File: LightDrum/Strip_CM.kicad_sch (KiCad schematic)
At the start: 10 parts, among them U42 INA4181 A2, U43 INA4181 A2

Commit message: Add docs and gerbers for REV7
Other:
- title: RGB CURRENT MONITORS -> LightDrum
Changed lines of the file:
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@@
   (paper "A4")
   (title_block
-    (title "RGB CURRENT MONITORS")
-    (rev "REV6")
+    (title "LightDrum")
+    (rev "REV7")
     (company "Daxxn Industries")
   )

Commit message: First pass over schematic (WIP)
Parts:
- R108, R109, R110, R111, R112, R113, R114, R115: value 60m${RES} -> 60m
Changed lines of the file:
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@@
   (title_block
     (title "LightDrum")
-    (rev "REV7")
+    (rev "REV8")
     (company "Daxxn Industries")
   )
@@
       (effects (font (size 1.27 1.27)) hide)
     )
-    (property "Datasheet" "C:\\Users\\Daxxn\\Documents\\Electrical\\Datasheets\\INA181.pdf" (id 3) (at 90.17 53.34 0)
+    (property "Datasheet" "%LOCAL_DATASHEETS%\\INA181.pdf" (id 3) (at 90.17 53.34 0)
       (effects (font (size 1.27 1.27)) hide)
     )
@@
     (in_bom yes) (on_board yes)
     (property "Reference" "R115" (id 0) (at 77.47 102.87 90))
-    (property "Value" "60m${RES}" (id 1) (at 77.47 104.648 90))
+    (property "Value" "60m" (id 1) (at 77.47 104.648 90))
     (property "Footprint" "Resistor_SMD:R_2010_5025Metric" (id 2) (at 77.724 105.664 90)
       (effects (font (size 1.27 1.27)) hide)
@@
     (in_bom yes) (on_board yes)
     (property "Reference" "R114" (id 0) (at 77.47 77.47 90))
-    (property "Value" "60m${RES}" (id 1) (at 77.47 79.248 90))
+    (property "Value" "60m" (id 1) (at 77.47 79.248 90))
     (property "Footprint" "Resistor_SMD:R_2010_5025Metric" (id 2) (at 77.724 80.264 90)
       (effects (font (size 1.27 1.27)) hide)
@@
       (effects (font (size 1.27 1.27)) hide)
     )
-    (property "Datasheet" "C:\\Users\\Daxxn\\Documents\\Electrical\\Datasheets\\INA181.pdf" (id 3) (at 90.17 27.94 0)
+    (property "Datasheet" "%LOCAL_DATASHEETS%\\INA181.pdf" (id 3) (at 90.17 27.94 0)
       (effects (font (size 1.27 1.27)) hide)
     )
@@
       (effects (font (size 1.27 1.27)) hide)
     )
-    (property "Datasheet" "C:\\Users\\Daxxn\\Documents\\Electrical\\Datasheets\\INA181.pdf" (id 3) (at 39.37 27.94 0)
+    (property "Datasheet" "%LOCAL_DATASHEETS%\\INA181.pdf" (id 3) (at 39.37 27.94 0)
       (effects (font (size 1.27 1.27)) hide)
     )
@@
     (in_bom yes) (on_board yes)
     (property "Reference" "R110" (id 0) (at 26.67 77.47 90))
-    (property "Value" "60m${RES}" (id 1) (at 26.67 79.248 90))
+    (property "Value" "60m" (id 1) (at 26.67 79.248 90))
     (property "Footprint" "Resistor_SMD:R_2010_5025Metric" (id 2) (at 26.924 80.264 90)
       (effects (font (size 1.27 1.27)) hide)
@@
       (effects (font (size 1.27 1.27)) hide)
     )
-    (property "Datasheet" "C:\\Users\\Daxxn\\Documents\\Electrical\\Datasheets\\INA181.pdf" (id 3) (at 39.37 104.14 0)
+    (property "Datasheet" "%LOCAL_DATASHEETS%\\INA181.pdf" (id 3) (at 39.37 104.14 0)
       (effects (font (size 1.27 1.27)) hide)
     )
@@
       (effects (font (size 1.27 1.27)) hide)
     )
-    (property "Datasheet" "C:\\Users\\Daxxn\\Documents\\Electrical\\Datasheets\\INA181.pdf" (id 3) (at 90.17 78.74 0)
+    (property "Datasheet" "%LOCAL_DATASHEETS%\\INA181.pdf" (id 3) (at 90.17 78.74 0)
       (effects (font (size 1.27 1.27)) hide)
     )
@@
     (in_bom yes) (on_board yes)
     (property "Reference" "R113" (id 0) (at 77.47 52.07 90))
-    (property "Value" "60m${RES}" (id 1) (at 77.47 53.848 90))
+    (property "Value" "60m" (id 1) (at 77.47 53.848 90))
     (property "Footprint" "Resistor_SMD:R_2010_5025Metric" (id 2) (at 77.724 54.864 90)
       (effects (font (size 1.27 1.27)) hide)
@@
       (effects (font (size 1.27 1.27)) hide)
     )
-    (property "Datasheet" "C:\\Users\\Daxxn\\Documents\\Electrical\\Datasheets\\INA181.pdf" (id 3) (at 90.17 104.14 0)
+    (property "Datasheet" "%LOCAL_DATASHEETS%\\INA181.pdf" (id 3) (at 90.17 104.14 0)
       (effects (font (size 1.27 1.27)) hide)
     )
@@
       (effects (font (size 1.27 1.27)) hide)
     )
-    (property "Datasheet" "C:\\Users\\Daxxn\\Documents\\Electrical\\Datasheets\\INA181.pdf" (id 3) (at 39.37 53.34 0)
+    (property "Datasheet" "%LOCAL_DATASHEETS%\\INA181.pdf" (id 3) (at 39.37 53.34 0)
       (effects (font (size 1.27 1.27)) hide)
     )
@@
     (in_bom yes) (on_board yes)
     (property "Reference" "R108" (id 0) (at 26.67 26.67 90))
-    (property "Value" "60m${RES}" (id 1) (at 26.67 28.448 90))
+    (property "Value" "60m" (id 1) (at 26.67 28.448 90))
     (property "Footprint" "Resistor_SMD:R_2010_5025Metric" (id 2) (at 26.924 29.464 90)
       (effects (font (size 1.27 1.27)) hide)
@@
       (effects (font (size 1.27 1.27)) hide)
     )
-    (property "Datasheet" "C:\\Users\\Daxxn\\Documents\\Electrical\\Datasheets\\INA181.pdf" (id 3) (at 39.37 78.74 0)
+    (property "Datasheet" "%LOCAL_DATASHEETS%\\INA181.pdf" (id 3) (at 39.37 78.74 0)
       (effects (font (size 1.27 1.27)) hide)
     )
@@
     (in_bom yes) (on_board yes)
     (property "Reference" "R109" (id 0) (at 26.67 52.07 90))
-    (property "Value" "60m${RES}" (id 1) (at 26.67 53.848 90))
+    (property "Value" "60m" (id 1) (at 26.67 53.848 90))
     (property "Footprint" "Resistor_SMD:R_2010_5025Metric" (id 2) (at 26.924 54.864 90)
       (effects (font (size 1.27 1.27)) hide)
@@
     (in_bom yes) (on_board yes)
     (property "Reference" "R111" (id 0) (at 26.67 102.87 90))
-    (property "Value" "60m${RES}" (id 1) (at 26.67 104.648 90))
+    (property "Value" "60m" (id 1) (at 26.67 104.648 90))
     (property "Footprint" "Resistor_SMD:R_2010_5025Metric" (id 2) (at 26.924 105.664 90)
       (effects (font (size 1.27 1.27)) hide)
@@
     (in_bom yes) (on_board yes)
     (property "Reference" "R112" (id 0) (at 77.47 26.67 90))
-    (property "Value" "60m${RES}" (id 1) (at 77.47 28.448 90))
+    (property "Value" "60m" (id 1) (at 77.47 28.448 90))
     (property "Footprint" "Resistor_SMD:R_2010_5025Metric" (id 2) (at 77.724 29.464 90)
       (effects (font (size 1.27 1.27)) hide)

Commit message: General component placement
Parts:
- U701: renamed from U42; PartNumber (none) -> 0815-0003
- U702: renamed from U43; PartNumber (none) -> 0815-0003
- renumbered R108 to R701, R112 to R702, R109 to R703, R113 to R704, R110 to R705, R114 to R706, R111 to R707, R115 to R708

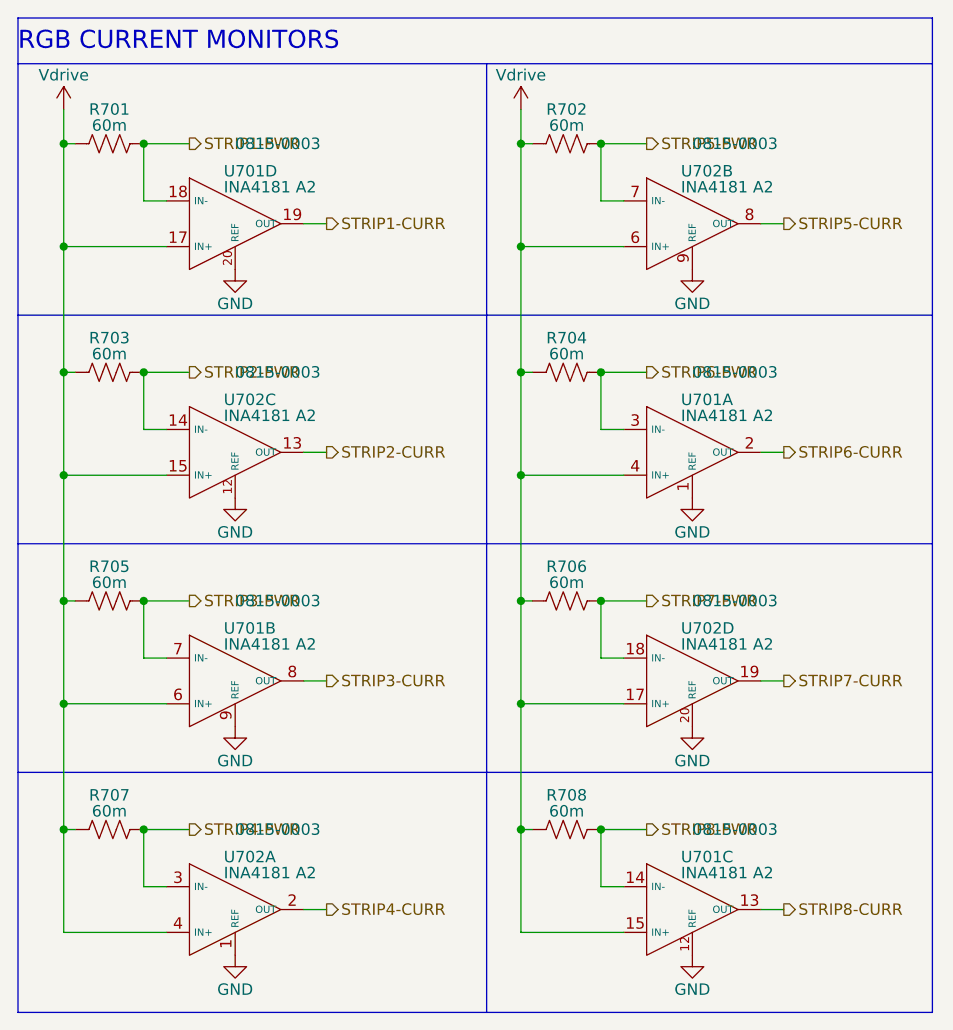
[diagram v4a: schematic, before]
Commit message: Simplify analog power supply and add some routing
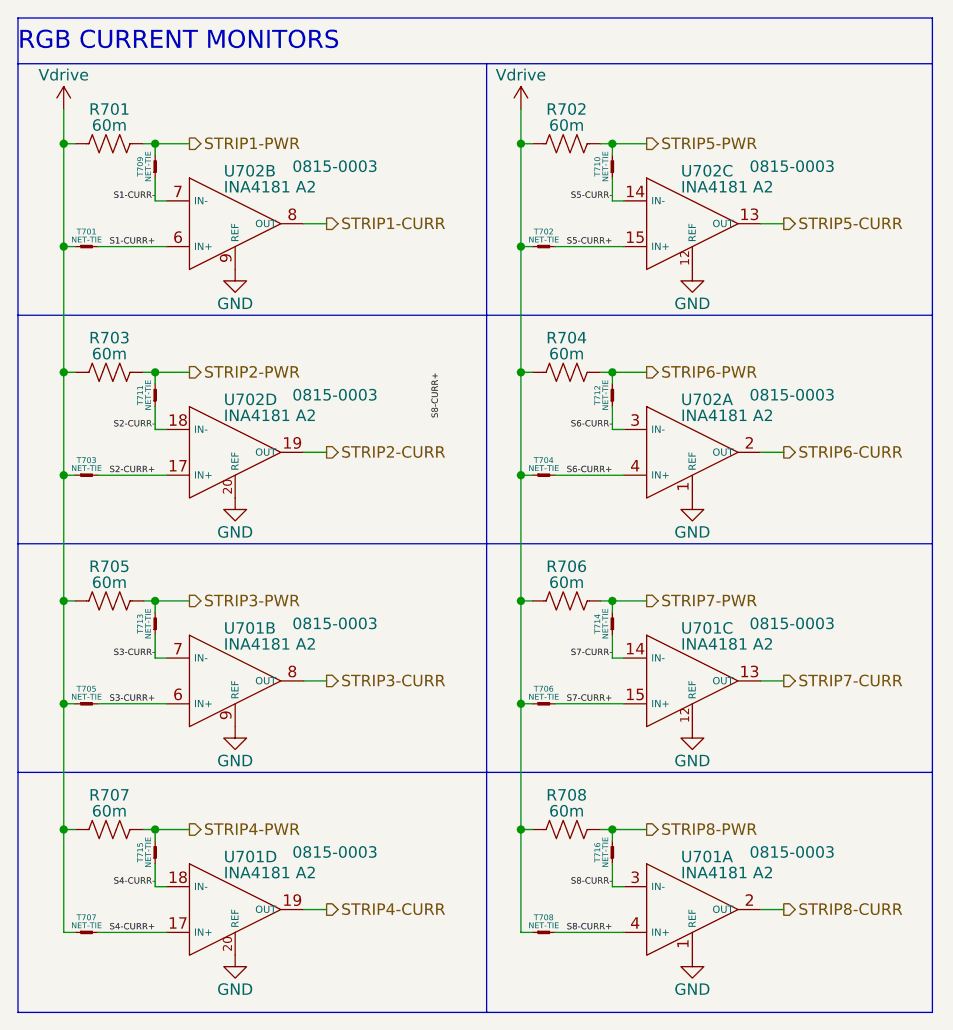
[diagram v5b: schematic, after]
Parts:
- added T701, T702, T703, T704, T705, T706, T707, T708, T709, T710, T711, T712, T713, T714, T715, T716: NET-TIE, Daxxn_Other:NetTie-2_SMD_Pad0.25mm, symbol Daxxn_Other:NET-TIE
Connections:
- net STRIP1-CURR: now also U702.8 (OUT); no longer U701.19 (OUT)
- net STRIP1-PWR: now also T709.2; no longer U701.18 (IN-)
- net STRIP2-CURR: now also U702.19 (OUT); no longer U702.13 (OUT)
- net STRIP2-PWR: now also T711.2; no longer U702.14 (IN-)
- net STRIP3-PWR: now also T713.2; no longer U701.7 (IN-)
- net STRIP4-CURR: now also U701.19 (OUT); no longer U702.2 (OUT)
- net STRIP4-PWR: now also T715.2; no longer U702.3 (IN-)
- net STRIP5-CURR: now also U702.13 (OUT); no longer U702.8 (OUT)
- net STRIP5-PWR: now also T710.2; no longer U702.7 (IN-)
- net STRIP6-CURR: now also U702.2 (OUT); no longer U701.2 (OUT)
- net STRIP6-PWR: now also T712.2; no longer U701.3 (IN-)
- net STRIP7-CURR: now also U701.13 (OUT); no longer U702.19 (OUT)
- net STRIP7-PWR: now also T714.2; no longer U702.18 (IN-)
- net STRIP8-CURR: now also U701.2 (OUT); no longer U701.13 (OUT)
- net STRIP8-PWR: now also T716.2; no longer U701.14 (IN-)
- net Vdrive: now also T701.1, T702.1, T703.1, T704.1, T705.1, T706.1, T707.1, T708.1; no longer U701.15 (IN+), U701.17 (IN+), U701.4 (IN+), U701.6 (IN+), U702.15 (IN+), U702.17 (IN+), U702.4 (IN+), U702.6 (IN+)
- new net S1-CURR+: T701.2, U702.6 (IN+)
- new net S1-CURR-: T709.1, U702.7 (IN-)
- new net S2-CURR+: T703.2, U702.17 (IN+)
- new net S2-CURR-: T711.1, U702.18 (IN-)
- new net S3-CURR+: T705.2, U701.6 (IN+)
- new net S3-CURR-: T713.1, U701.7 (IN-)
- new net S4-CURR+: T707.2, U701.17 (IN+)
- new net S4-CURR-: T715.1, U701.18 (IN-)
- new net S5-CURR+: T702.2, U702.15 (IN+)
- new net S5-CURR-: T710.1, U702.14 (IN-)
- new net S6-CURR+: T704.2, U702.4 (IN+)
- new net S6-CURR-: T712.1, U702.3 (IN-)
- new net S7-CURR+: T706.2, U701.15 (IN+)
- new net S7-CURR-: T714.1, U701.14 (IN-)
- new net S8-CURR+: T708.2, U701.4 (IN+)
- new net S8-CURR-: T716.1, U701.3 (IN-)
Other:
- moved on the sheet: U701A, U701C, U701D, U702A, U702B, U702C, U702D

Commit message: interface layout completed - REV6
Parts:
- R701, R702, R703, R704, R705, R706, R707, R708: value 60m -> 50m
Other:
- note added: "STRIP 1"
- note added: "STRIP 2"
- note added: "STRIP 3"
- note added: "STRIP 4"
- note added: "STRIP 5"
- note added: "STRIP 6"
- note added: "STRIP 7"
- note added: "STRIP 8"
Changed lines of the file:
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@@
+    (stroke (width 0) (type default) (color 0 0 0 0))
+  )
+  (polyline (pts (xy 68.58 77.47) (xy 58.42 77.47))
     (stroke (width 0) (type default) (color 0 0 0 0))
   )
@@
     (stroke (width 0) (type default) (color 0 0 0 0))
   )
+  (polyline (pts (xy 107.95 52.07) (xy 107.95 49.53))
+    (stroke (width 0) (type default) (color 0 0 0 0))
+  )
   (polyline (pts (xy 16.51 21.59) (xy 118.11 21.59))
     (stroke (width 0) (type default) (color 0 0 0 0))
@@
     (stroke (width 0) (type default) (color 0 0 0 0))
   )
+  (polyline (pts (xy 107.95 24.13) (xy 107.95 21.59))
+    (stroke (width 0) (type default) (color 0 0 0 0))
+  )
   (wire (pts (xy 31.75 30.48) (xy 35.56 30.48))
     (stroke (width 0) (type default) (color 0 0 0 0))
@@
     (stroke (width 0) (type default) (color 0 0 0 0))
   )
+  (polyline (pts (xy 68.58 102.87) (xy 58.42 102.87))
+    (stroke (width 0) (type default) (color 0 0 0 0))
+  )
   (wire (pts (xy 25.4 118.11) (xy 33.02 118.11))
     (stroke (width 0) (type default) (color 0 0 0 0))
   )
+  (polyline (pts (xy 118.11 77.47) (xy 107.95 77.47))
+    (stroke (width 0) (type default) (color 0 0 0 0))
+  )
   (wire (pts (xy 81.28 106.68) (xy 82.55 106.68))
     (stroke (width 0) (type default) (color 0 0 0 0))
@@
     (stroke (width 0) (type default) (color 0 0 0 0))
   )
+  (polyline (pts (xy 107.95 102.87) (xy 107.95 100.33))
+    (stroke (width 0) (type default) (color 0 0 0 0))
+  )
+  (polyline (pts (xy 68.58 24.13) (xy 58.42 24.13))
+    (stroke (width 0) (type default) (color 0 0 0 0))
+  )
   (wire (pts (xy 48.26 64.77) (xy 50.8 64.77))
     (stroke (width 0) (type default) (color 0 0 0 0))
@@
     (stroke (width 0) (type default) (color 0 0 0 0))
   )
+  (polyline (pts (xy 118.11 102.87) (xy 107.95 102.87))
+    (stroke (width 0) (type default) (color 0 0 0 0))
+  )
   (wire (pts (xy 81.28 30.48) (xy 82.55 30.48))
     (stroke (width 0) (type default) (color 0 0 0 0))
@@
     (stroke (width 0) (type default) (color 0 0 0 0))
   )
+  (polyline (pts (xy 58.42 24.13) (xy 58.42 21.59))
+    (stroke (width 0) (type default) (color 0 0 0 0))
+  )
   (wire (pts (xy 31.75 106.68) (xy 31.75 107.95))
     (stroke (width 0) (type default) (color 0 0 0 0))
@@
     (stroke (width 0) (type default) (color 0 0 0 0))
   )
+  (polyline (pts (xy 58.42 77.47) (xy 58.42 74.93))
+    (stroke (width 0) (type default) (color 0 0 0 0))
+  )
   (wire (pts (xy 21.59 118.11) (xy 22.86 118.11))
     (stroke (width 0) (type default) (color 0 0 0 0))
@@
     (stroke (width 0) (type default) (color 0 0 0 0))
   )
+  (polyline (pts (xy 58.42 52.07) (xy 58.42 49.53))
+    (stroke (width 0) (type default) (color 0 0 0 0))
+  )
   (wire (pts (xy 31.75 81.28) (xy 35.56 81.28))
     (stroke (width 0) (type default) (color 0 0 0 0))
@@
     (stroke (width 0) (type default) (color 0 0 0 0))
   )
+  (polyline (pts (xy 58.42 102.87) (xy 58.42 100.33))
+    (stroke (width 0) (type default) (color 0 0 0 0))
+  )
   (wire (pts (xy 31.75 81.28) (xy 31.75 82.55))
     (stroke (width 0) (type default) (color 0 0 0 0))
@@
     (stroke (width 0) (type default) (color 0 0 0 0))
   )
+  (polyline (pts (xy 118.11 52.07) (xy 107.95 52.07))
+    (stroke (width 0) (type default) (color 0 0 0 0))
+  )
   (wire (pts (xy 72.39 81.28) (xy 73.66 81.28))
     (stroke (width 0) (type default) (color 0 0 0 0))
@@
     (stroke (width 0) (type default) (color 0 0 0 0))
   )
+  (polyline (pts (xy 107.95 77.47) (xy 107.95 74.93))
+    (stroke (width 0) (type default) (color 0 0 0 0))
+  )
   (wire (pts (xy 81.28 81.28) (xy 82.55 81.28))
     (stroke (width 0) (type default) (color 0 0 0 0))
   )
+  (polyline (pts (xy 118.11 24.13) (xy 107.95 24.13))
+    (stroke (width 0) (type default) (color 0 0 0 0))
+  )
   (wire (pts (xy 31.75 59.69) (xy 31.75 62.23))
     (stroke (width 0) (type default) (color 0 0 0 0))
@@
     (stroke (width 0) (type default) (color 0 0 0 0))
   )
+  (polyline (pts (xy 68.58 52.07) (xy 58.42 52.07))
+    (stroke (width 0) (type default) (color 0 0 0 0))
+  )
   (polyline (pts (xy 16.51 49.53) (xy 118.11 49.53))
     (stroke (width 0) (type default) (color 0 0 0 0))
@@
   (wire (pts (xy 48.26 115.57) (xy 50.8 115.57))
     (stroke (width 0) (type default) (color 0 0 0 0))
+  )
+  (text "STRIP 8" (at 117.856 102.87 180)
+    (effects (font (size 1.5 1.5) (thickness 0.2) bold) (justify right bottom))
+  )
+  (text "STRIP 5" (at 117.856 24.13 180)
+    (effects (font (size 1.5 1.5) (thickness 0.2) bold) (justify right bottom))
+  )
+  (text "STRIP 3" (at 68.326 77.47 180)
+    (effects (font (size 1.5 1.5) (thickness 0.2) bold) (justify right bottom))
+  )
+  (text "STRIP 4" (at 68.326 102.87 180)
+    (effects (font (size 1.5 1.5) (thickness 0.2) bold) (justify right bottom))
+  )
+  (text "STRIP 1" (at 68.326 24.13 180)
+    (effects (font (size 1.5 1.5) (thickness 0.2) bold) (justify right bottom))
   )
   (text "RGB CURRENT MONITORS" (at 16.51 20.32 0)
     (effects (font (size 2 2)) (justify left bottom))
   )
+  (text "STRIP 7" (at 117.856 77.47 180)
+    (effects (font (size 1.5 1.5) (thickness 0.2) bold) (justify right bottom))
+  )
+  (text "STRIP 2" (at 68.326 52.07 180)
+    (effects (font (size 1.5 1.5) (thickness 0.2) bold) (justify right bottom))
+  )
+  (text "STRIP 6" (at 117.856 52.07 180)
+    (effects (font (size 1.5 1.5) (thickness 0.2) bold) (justify right bottom))
+  )
   (label "S6-CURR+" (at 77.47 67.31 0)
     (effects (font (size 0.7 0.7)) (justify left bottom))
@@
   )
   (label "S7-CURR+" (at 77.47 92.71 0)
-    (effects (font (size 0.7 0.7)) (justify left bottom))
-  )
-  (label "S8-CURR+" (at 63.5 60.96 90)
     (effects (font (size 0.7 0.7)) (justify left bottom))
   )
@@
     (in_bom yes) (on_board yes)
     (property "Reference" "R708" (id 0) (at 77.47 102.87 90))
-    (property "Value" "60m" (id 1) (at 77.47 104.648 90))
+    (property "Value" "50m" (id 1) (at 77.47 104.648 90))
     (property "Footprint" "Resistor_SMD:R_2010_5025Metric" (id 2) (at 77.724 105.664 90)
       (effects (font (size 1.27 1.27)) hide)
@@
     (in_bom yes) (on_board yes)
     (property "Reference" "R706" (id 0) (at 77.47 77.47 90))
-    (property "Value" "60m" (id 1) (at 77.47 79.248 90))
+    (property "Value" "50m" (id 1) (at 77.47 79.248 90))
     (property "Footprint" "Resistor_SMD:R_2010_5025Metric" (id 2) (at 77.724 80.264 90)
       (effects (font (size 1.27 1.27)) hide)
@@
     (in_bom yes) (on_board yes)
     (property "Reference" "R705" (id 0) (at 26.67 77.47 90))
-    (property "Value" "60m" (id 1) (at 26.67 79.248 90))
+    (property "Value" "50m" (id 1) (at 26.67 79.248 90))
     (property "Footprint" "Resistor_SMD:R_2010_5025Metric" (id 2) (at 26.924 80.264 90)
       (effects (font (size 1.27 1.27)) hide)
@@
     (in_bom yes) (on_board yes)
     (property "Reference" "R704" (id 0) (at 77.47 52.07 90))
-    (property "Value" "60m" (id 1) (at 77.47 53.848 90))
+    (property "Value" "50m" (id 1) (at 77.47 53.848 90))
     (property "Footprint" "Resistor_SMD:R_2010_5025Metric" (id 2) (at 77.724 54.864 90)
       (effects (font (size 1.27 1.27)) hide)
@@
     (in_bom yes) (on_board yes)
     (property "Reference" "R701" (id 0) (at 26.67 26.67 90))
-    (property "Value" "60m" (id 1) (at 26.67 28.448 90))
+    (property "Value" "50m" (id 1) (at 26.67 28.448 90))
     (property "Footprint" "Resistor_SMD:R_2010_5025Metric" (id 2) (at 26.924 29.464 90)
       (effects (font (size 1.27 1.27)) hide)
@@
     (in_bom yes) (on_board yes)
     (property "Reference" "R703" (id 0) (at 26.67 52.07 90))
-    (property "Value" "60m" (id 1) (at 26.67 53.848 90))
+    (property "Value" "50m" (id 1) (at 26.67 53.848 90))
     (property "Footprint" "Resistor_SMD:R_2010_5025Metric" (id 2) (at 26.924 54.864 90)
       (effects (font (size 1.27 1.27)) hide)
@@
     (in_bom yes) (on_board yes)
     (property "Reference" "R707" (id 0) (at 26.67 102.87 90))
-    (property "Value" "60m" (id 1) (at 26.67 104.648 90))
+    (property "Value" "50m" (id 1) (at 26.67 104.648 90))
     (property "Footprint" "Resistor_SMD:R_2010_5025Metric" (id 2) (at 26.924 105.664 90)
       (effects (font (size 1.27 1.27)) hide)
@@
     (in_bom yes) (on_board yes)
     (property "Reference" "R702" (id 0) (at 77.47 26.67 90))
-    (property "Value" "60m" (id 1) (at 77.47 28.448 90))
+    (property "Value" "50m" (id 1) (at 77.47 28.448 90))
     (property "Footprint" "Resistor_SMD:R_2010_5025Metric" (id 2) (at 77.724 29.464 90)
       (effects (font (size 1.27 1.27)) hide)
